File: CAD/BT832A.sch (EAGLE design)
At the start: 22 parts, among them IC1 CP2102, U2 BT832, U3 LP5907MFX-3.3/NOPB, U4 LP5907MFX-3.3/NOPB, U5 ADS131M08IPBS, X1_8.192MHZ ABM3B-8.000MHZ-B2-T, X2_32.768KHZ FC-12M

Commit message: Update BT832A.sch
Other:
- note added: "TODO: Add 2.2uF caps between + and - inputs (at least for EEG)"
- note removed: "TODO: Add 220pf caps between + and - inputs."
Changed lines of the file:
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@@
 <text x="139.7" y="142.24" size="1.778" layer="97" rot="R90">830050789</text>
 <text x="127" y="38.1" size="1.778" layer="97">MicroUSB</text>
-<text x="-12.7" y="172.72" size="1.778" layer="95">TODO:
-Add 220pf caps between + and - inputs.</text>
+<text x="-12.7" y="170.18" size="1.778" layer="95">TODO:
+Add 2.2uF caps between + and - inputs
+(at least for EEG)</text>
 <wire x1="109.22" y1="25.4" x2="109.22" y2="76.2" width="0.1524" layer="97"/>
 <wire x1="109.22" y1="76.2" x2="50.8" y2="76.2" width="0.1524" layer="97"/>

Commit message: finished sch
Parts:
- added C10: 1.0uF, adafruit:C-USC0603
- added C11: 0.1uF, adafruit:C-USC0603
- added C12, C13: 1uF, adafruit:C-USC0603
- added D1: BAT60J, diode:BAT60J
- added D2, D3: BAS40-06, diode:BAS40-06
- added LED1, LED2: (no value), adafruit:LEDCHIP-LED0603
- added R1: 4.7kΩ, adafruit:R-US_R0603
- added R2, R3: 3.3kΩ, adafruit:R-US_R0603
- added R4, R7: 10kΩ, adafruit:R-US_R0603
- added R5: 47kΩ, adafruit:R-US_R0603
- added R6: 2kΩ, adafruit:R-US_R0603
- added U1: MCP73831T-3ACI/OT, MCP73831T-3ACI_OT:MCP73831T-3ACI/OT
- added U6: BCM857BS, BCM857BS:BCM857BS
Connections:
- new net +5V: C10.2, C11.2, C7.1, D2.AA, IC1.REGIN, IC1.VBUS, U$1.1, U4.EN, U4.IN, U6.E1
- new net 10K: R4.2, U6.B1, U6.B2, U6.C1
- new net B+: D3.AA, J1.+
- new net CPRST: IC1.!RST, R1.1, U2.P08
- new net D+: IC1.D+, U$1.3
- new net D-: IC1.D-, U$1.2
- new net ID: U$1.4
- new net N$1: LED2.A, R3.1
- new net N$11: LED1.A, R2.2
- new net N$14: D2.K2, R5.1, U6.C2
- new net N$18: LED1.C, U1.STAT
- new net N$2: U2.P21/RESET
- new net N$3: LED2.C
- new net N$4: U2.VDD
- new net N$5: R3.2
- new net N$8: U3.GND
- new net N$9: R6.1, U1.PROG
- new net NVD: D1.A, D2.K1, D3.K2, R2.1, R7.2, U1.VDD, U6.E2
- new net RXD: IC1.RXD, U2.P12
- new net TXD: IC1.TXD, U2.P11
- new net VDD: C12.2, R1.2, U3.OUT
- new net VIN: C13.2, D1.C, D3.K1, U3.EN, U3.IN
- net 3V3: no longer C7.1, U4.EN, U4.IN
- net GND: now also C10.1, C11.1, C12.1, C13.1, IC1.GND, IC1.GND@EXP, IC1.GND@M, J1.-, R4.1, R5.2, R6.2, R7.1, U$1.5, U2.GND
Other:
- moved on the sheet: J1

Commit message: smaller packages
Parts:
- C10, C11, C12, C13, C5, C6, C7, C8, C9: device adafruit:C-USC0603 -> adafruit:C-USC0402
- R1, R2, R3, R4, R5, R6: device adafruit:R-US_R0603 -> adafruit:R-US_R0402
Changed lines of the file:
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@@
 <part name="J1" library="SparkFun-Connectors" library_urn="urn:adsk.eagle:library:513" deviceset="JST_2MM_MALE" device="" package3d_urn="urn:adsk.eagle:package:38042/1"/>
 <part name="U4" library="LP5907MFX-3.3_NOPB" deviceset="LP5907MFX-3.3/NOPB" device=""/>
-<part name="C5" library="adafruit" deviceset="C-US" device="C0603" value="1uF"/>
-<part name="C6" library="adafruit" deviceset="C-US" device="C0603" value="220uF"/>
-<part name="C7" library="adafruit" deviceset="C-US" device="C0603" value="1uF"/>
-<part name="C8" library="adafruit" deviceset="C-US" device="C0603" value="1uF"/>
+<part name="C5" library="adafruit" deviceset="C-US" device="C0402" value="1uF"/>
+<part name="C6" library="adafruit" deviceset="C-US" device="C0402" value="220uF"/>
+<part name="C7" library="adafruit" deviceset="C-US" device="C0402" value="1uF"/>
+<part name="C8" library="adafruit" deviceset="C-US" device="C0402" value="1uF"/>
 <part name="SV1" library="con-lsta" library_urn="urn:adsk.eagle:library:161" deviceset="FE08-2" device="" package3d_urn="urn:adsk.eagle:package:8174/1"/>
 <part name="U5" library="ADS131M08IPBS" deviceset="ADS131M08IPBS" device=""/>
-<part name="C9" library="adafruit" deviceset="C-US" device="C0603" value="100uF"/>
+<part name="C9" library="adafruit" deviceset="C-US" device="C0402" value="100uF"/>
 <part name="SJ1" library="jumper" library_urn="urn:adsk.eagle:library:252" deviceset="SJ" device="" package3d_urn="urn:adsk.eagle:package:15471/1"/>
 <part name="U$2" library="adafruit" deviceset="PINHD-1X10" device=""/>
@@
 <part name="SUPPLY1" library="supply2" library_urn="urn:adsk.eagle:library:372" deviceset="GND" device=""/>
 <part name="SUPPLY2" library="supply2" library_urn="urn:adsk.eagle:library:372" deviceset="GND" device=""/>
-<part name="C10" library="adafruit" library_urn="urn:adsk.eagle:library:420" deviceset="C-US" device="C0603" package3d_urn="urn:adsk.eagle:package:6240338/1" value="1.0uF"/>
-<part name="C11" library="adafruit" library_urn="urn:adsk.eagle:library:420" deviceset="C-US" device="C0603" package3d_urn="urn:adsk.eagle:package:6240338/1" value="0.1uF"/>
+<part name="C10" library="adafruit" library_urn="urn:adsk.eagle:library:420" deviceset="C-US" device="C0402" package3d_urn="urn:adsk.eagle:package:6240340/1" value="1.0uF"/>
+<part name="C11" library="adafruit" library_urn="urn:adsk.eagle:library:420" deviceset="C-US" device="C0402" package3d_urn="urn:adsk.eagle:package:6240340/1" value="0.1uF"/>
 <part name="P+1" library="supply1" library_urn="urn:adsk.eagle:library:371" deviceset="+5V" device=""/>
 <part name="SUPPLY3" library="supply2" library_urn="urn:adsk.eagle:library:372" deviceset="GND" device=""/>
 <part name="P+2" library="supply1" library_urn="urn:adsk.eagle:library:371" deviceset="+5V" device=""/>
 <part name="P+3" library="supply1" library_urn="urn:adsk.eagle:library:371" deviceset="+5V" device=""/>
-<part name="R1" library="adafruit" library_urn="urn:adsk.eagle:library:420" deviceset="R-US_" device="R0603" package3d_urn="urn:adsk.eagle:package:6240565/1" value="4.7kΩ"/>
-<part name="C12" library="adafruit" deviceset="C-US" device="C0603" value="1uF"/>
-<part name="C13" library="adafruit" deviceset="C-US" device="C0603" value="1uF"/>
+<part name="R1" library="adafruit" library_urn="urn:adsk.eagle:library:420" deviceset="R-US_" device="R0402" package3d_urn="urn:adsk.eagle:package:6240564/1" value="4.7kΩ"/>
+<part name="C12" library="adafruit" deviceset="C-US" device="C0402" value="1uF"/>
+<part name="C13" library="adafruit" deviceset="C-US" device="C0402" value="1uF"/>
 <part name="SUPPLY4" library="supply2" library_urn="urn:adsk.eagle:library:372" deviceset="GND" device=""/>
 <part name="U1" library="MCP73831T-3ACI_OT" deviceset="MCP73831T-3ACI/OT" device=""/>
@@
 <part name="LED1" library="adafruit" library_urn="urn:adsk.eagle:library:420" deviceset="LED" device="CHIP-LED0603" package3d_urn="urn:adsk.eagle:package:6240556/1"/>
 <part name="LED2" library="adafruit" library_urn="urn:adsk.eagle:library:420" deviceset="LED" device="CHIP-LED0603" package3d_urn="urn:adsk.eagle:package:6240556/1"/>
-<part name="R2" library="adafruit" library_urn="urn:adsk.eagle:library:420" deviceset="R-US_" device="R0603" package3d_urn="urn:adsk.eagle:package:6240565/1" value="3.3kΩ"/>
-<part name="R3" library="adafruit" library_urn="urn:adsk.eagle:library:420" deviceset="R-US_" device="R0603" package3d_urn="urn:adsk.eagle:package:6240565/1" value="3.3kΩ"/>
-<part name="R4" library="adafruit" library_urn="urn:adsk.eagle:library:420" deviceset="R-US_" device="R0603" package3d_urn="urn:adsk.eagle:package:6240565/1" value="10kΩ"/>
-<part name="R5" library="adafruit" library_urn="urn:adsk.eagle:library:420" deviceset="R-US_" device="R0603" package3d_urn="urn:adsk.eagle:package:6240565/1" value="47kΩ"/>
-<part name="R6" library="adafruit" library_urn="urn:adsk.eagle:library:420" deviceset="R-US_" device="R0603" package3d_urn="urn:adsk.eagle:package:6240565/1" value="2kΩ"/>
+<part name="R2" library="adafruit" library_urn="urn:adsk.eagle:library:420" deviceset="R-US_" device="R0402" package3d_urn="urn:adsk.eagle:package:6240564/1" value="3.3kΩ"/>
+<part name="R3" library="adafruit" library_urn="urn:adsk.eagle:library:420" deviceset="R-US_" device="R0402" package3d_urn="urn:adsk.eagle:package:6240564/1" value="3.3kΩ"/>
+<part name="R4" library="adafruit" library_urn="urn:adsk.eagle:library:420" deviceset="R-US_" device="R0402" package3d_urn="urn:adsk.eagle:package:6240564/1" value="10kΩ"/>
+<part name="R5" library="adafruit" library_urn="urn:adsk.eagle:library:420" deviceset="R-US_" device="R0402" package3d_urn="urn:adsk.eagle:package:6240564/1" value="47kΩ"/>
+<part name="R6" library="adafruit" library_urn="urn:adsk.eagle:library:420" deviceset="R-US_" device="R0402" package3d_urn="urn:adsk.eagle:package:6240564/1" value="2kΩ"/>
 <part name="P+4" library="supply1" library_urn="urn:adsk.eagle:library:371" deviceset="+5V" device=""/>
 <part name="SUPPLY5" library="supply2" library_urn="urn:adsk.eagle:library:372" deviceset="GND" device=""/>

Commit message: edits
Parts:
- renumbered X1_8.192MHZ to X1, X2_32.768KHZ to X2
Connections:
- new net SWDCLK: U2.SWDCLK
- new net SWDIO: U2.SWDIO
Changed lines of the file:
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@@
 <part name="U2" library="BT832" deviceset="BT832" device=""/>
 <part name="U3" library="LP5907MFX-3.3_NOPB" deviceset="LP5907MFX-3.3/NOPB" device=""/>
-<part name="X2_32.768KHZ" library="crystal" library_urn="urn:adsk.eagle:library:204" deviceset="FC-12M" device="" package3d_urn="urn:adsk.eagle:package:12123/1"/>
-<part name="X1_8.192MHZ" library="Crystals_Oscillators" library_urn="urn:adsk.eagle:library:24014151" deviceset="ABM3B-8.000MHZ-B2-T" device="" package3d_urn="urn:adsk.eagle:package:10899604/4"/>
+<part name="X2" library="crystal" library_urn="urn:adsk.eagle:library:204" deviceset="FC-12M" device="" package3d_urn="urn:adsk.eagle:package:12123/1"/>
+<part name="X1" library="Crystals_Oscillators" library_urn="urn:adsk.eagle:library:24014151" deviceset="ABM3B-8.000MHZ-B2-T" device="" package3d_urn="urn:adsk.eagle:package:10899604/4"/>
 <part name="C1" library="adafruit" library_urn="urn:adsk.eagle:library:420" deviceset="C-US" device="C0402" package3d_urn="urn:adsk.eagle:package:6240340/1"/>
 <part name="C2" library="adafruit" library_urn="urn:adsk.eagle:library:420" deviceset="C-US" device="C0402" package3d_urn="urn:adsk.eagle:package:6240340/1"/>
@@
 <attribute name="VALUE" x="68.58" y="102.68" size="2.0828" layer="96" ratio="10" rot="SR0"/>
 </instance>
-<instance part="X2_32.768KHZ" gate="G$1" x="142.24" y="147.32" smashed="yes" rot="R90">
+<instance part="X2" gate="G$1" x="142.24" y="147.32" smashed="yes" rot="R90">
 <attribute name="NAME" x="136.144" y="139.7" size="1.778" layer="95" rot="R90"/>
 </instance>
-<instance part="X1_8.192MHZ" gate="G$1" x="-5.08" y="88.9" smashed="yes">
+<instance part="X1" gate="G$1" x="-5.08" y="88.9" smashed="yes">
 <attribute name="NAME" x="-8.128" y="69.85" size="1.778" layer="95"/>
 </instance>
@@
 </segment>
 <segment>
-<pinref part="X1_8.192MHZ" gate="G$1" pin="4"/>
+<pinref part="X1" gate="G$1" pin="4"/>
 <wire x1="0" y1="83.82" x2="0" y2="81.28" width="0.1524" layer="91"/>
 <label x="0" y="81.28" size="1.778" layer="95" rot="R270"/>
 </segment>
 <segment>
-<pinref part="X1_8.192MHZ" gate="G$1" pin="2"/>
+<pinref part="X1" gate="G$1" pin="2"/>
 <wire x1="-2.54" y1="83.82" x2="-2.54" y2="81.28" width="0.1524" layer="91"/>
 <label x="-2.54" y="81.28" size="1.778" layer="95" rot="R270"/>
@@
 </segment>
 <segment>
-<pinref part="X1_8.192MHZ" gate="G$1" pin="3"/>
+<pinref part="X1" gate="G$1" pin="3"/>
 <wire x1="5.08" y1="88.9" x2="7.62" y2="88.9" width="0.1524" layer="91"/>
 <label x="5.08" y="91.44" size="1.778" layer="95"/>
@@
 </segment>
 <segment>
-<pinref part="X1_8.192MHZ" gate="G$1" pin="1"/>
+<pinref part="X1" gate="G$1" pin="1"/>
 <wire x1="-7.62" y1="88.9" x2="-10.16" y2="88.9" width="0.1524" layer="91"/>
 <label x="-12.7" y="91.44" size="1.778" layer="95"/>
@@
 </segment>
 <segment>
-<pinref part="X2_32.768KHZ" gate="G$1" pin="2"/>
+<pinref part="X2" gate="G$1" pin="2"/>
 <wire x1="142.24" y1="149.86" x2="142.24" y2="152.4" width="0.1524" layer="91"/>
 <label x="142.24" y="152.4" size="1.778" layer="95"/>
@@
 </segment>
 <segment>
-<pinref part="X2_32.768KHZ" gate="G$1" pin="1"/>
+<pinref part="X2" gate="G$1" pin="1"/>
 <wire x1="142.24" y1="144.78" x2="142.24" y2="142.24" width="0.1524" layer="91"/>
 <label x="142.24" y="139.7" size="1.778" layer="95"/>
@@
 </segment>
 </net>
+<net name="SWDIO" class="0">
+<segment>
+<pinref part="U2" gate="G$1" pin="SWDIO"/>
+<wire x1="157.48" y1="101.6" x2="153.924" y2="101.6" width="0.1524" layer="91"/>
+<label x="144.526" y="100.838" size="1.778" layer="95"/>
+</segment>
+</net>
+<net name="SWDCLK" class="0">
+<segment>
+<pinref part="U2" gate="G$1" pin="SWDCLK"/>
+<wire x1="157.48" y1="104.14" x2="153.924" y2="104.14" width="0.1524" layer="91"/>
+<label x="142.748" y="103.378" size="1.778" layer="95"/>
+</segment>
+</net>

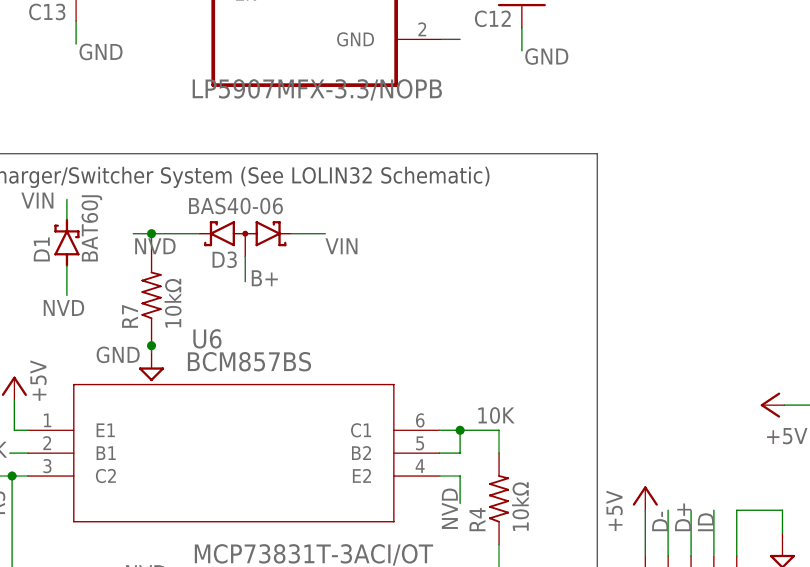
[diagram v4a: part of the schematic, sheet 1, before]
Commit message: add switch
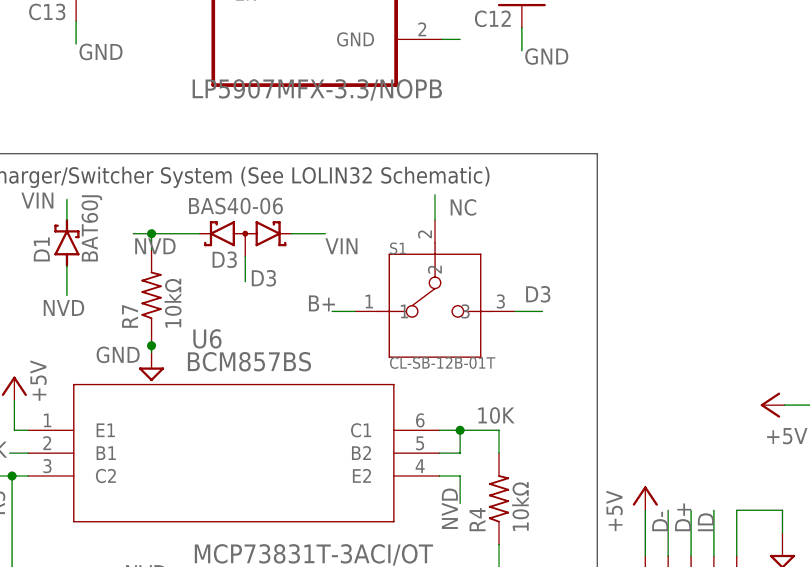
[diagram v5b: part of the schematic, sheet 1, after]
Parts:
- added S1: CL-SB-12B-01T, CL-SB-12B-01T:CL-SB-12B-01T
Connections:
- new net D3: D3.AA, S1.3
- net B+: now also S1.1; no longer D3.AA
- net NC: now also S1.2
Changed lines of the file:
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@@
 <part name="SUPPLY9" library="supply2" library_urn="urn:adsk.eagle:library:372" deviceset="GND" device=""/>
 <part name="P+5" library="supply1" library_urn="urn:adsk.eagle:library:371" deviceset="+5V" device=""/>
+<part name="S1" library="CL-SB-12B-01T" deviceset="CL-SB-12B-01T" device=""/>
 </parts>
 <sheets>
@@
 <attribute name="VALUE" x="52.578" y="68.834" size="1.778" layer="96" rot="R90"/>
 </instance>
+<instance part="S1" gate="A" x="95.758" y="78.994" smashed="yes">
+<attribute name="NAME" x="90.66451875" y="85.36085" size="1.27336875" layer="95" ratio="10"/>
+<attribute name="VALUE" x="90.66936875" y="72.633209375" size="1.27215" layer="96" ratio="10"/>
+</instance>
 </instances>
 <busses>
@@
 <label x="-46.99" y="108.966" size="1.778" layer="95"/>
 </segment>
+<segment>
+<pinref part="S1" gate="A" pin="2"/>
+<wire x1="95.758" y1="89.154" x2="95.758" y2="91.948" width="0.1524" layer="91"/>
+<label x="97.282" y="89.662" size="1.778" layer="95"/>
+</segment>
 </net>
 <net name="CAP" class="0">
@@
 </segment>
 <segment>
+<pinref part="S1" gate="A" pin="1"/>
+<wire x1="86.868" y1="78.994" x2="84.328" y2="78.994" width="0.1524" layer="91"/>
+<label x="81.534" y="78.994" size="1.778" layer="95"/>
+</segment>
+</net>
+<net name="VIN" class="0">
+<segment>
+<pinref part="U3" gate="G$1" pin="IN"/>
+<wire x1="66.04" y1="119.38" x2="63.754" y2="119.38" width="0.1524" layer="91"/>
+<label x="60.452" y="119.634" size="1.778" layer="95"/>
+</segment>
+<segment>
+<pinref part="U3" gate="G$1" pin="EN"/>
+<wire x1="66.04" y1="114.3" x2="63.754" y2="114.3" width="0.1524" layer="91"/>
+<label x="60.452" y="115.062" size="1.778" layer="95"/>
+</segment>
+<segment>
+<pinref part="D3" gate="G$1" pin="K1"/>
+<wire x1="79.756" y1="87.63" x2="83.566" y2="87.63" width="0.1524" layer="91"/>
+<label x="83.566" y="85.344" size="1.778" layer="95"/>
+</segment>
+<segment>
+<pinref part="D1" gate="G$1" pin="C"/>
+<wire x1="54.864" y1="89.154" x2="54.864" y2="91.44" width="0.1524" layer="91"/>
+<label x="49.784" y="90.424" size="1.778" layer="95"/>
+</segment>
+<segment>
+<pinref part="C13" gate="G$1" pin="2"/>
+<wire x1="55.88" y1="118.872" x2="55.88" y2="121.158" width="0.1524" layer="91"/>
+<label x="54.102" y="121.92" size="1.778" layer="95"/>
+</segment>
+</net>
+<net name="SWDIO" class="0">
+<segment>
+<pinref part="U2" gate="G$1" pin="SWDIO"/>
+<wire x1="157.48" y1="101.6" x2="153.924" y2="101.6" width="0.1524" layer="91"/>
+<label x="144.526" y="100.838" size="1.778" layer="95"/>
+</segment>
+</net>
+<net name="SWDCLK" class="0">
+<segment>
+<pinref part="U2" gate="G$1" pin="SWDCLK"/>
+<wire x1="157.48" y1="104.14" x2="153.924" y2="104.14" width="0.1524" layer="91"/>
+<label x="142.748" y="103.378" size="1.778" layer="95"/>
+</segment>
+</net>
+<net name="D3" class="0">
+<segment>
 <pinref part="D3" gate="G$1" pin="AA"/>
 <wire x1="74.676" y1="85.09" x2="74.676" y2="82.296" width="0.1524" layer="91"/>
 <label x="75.184" y="81.788" size="1.778" layer="95"/>
 </segment>
-</net>
-<net name="VIN" class="0">
-<segment>
-<pinref part="U3" gate="G$1" pin="IN"/>
-<wire x1="66.04" y1="119.38" x2="63.754" y2="119.38" width="0.1524" layer="91"/>
-<label x="60.452" y="119.634" size="1.778" layer="95"/>
-</segment>
-<segment>
-<pinref part="U3" gate="G$1" pin="EN"/>
-<wire x1="66.04" y1="114.3" x2="63.754" y2="114.3" width="0.1524" layer="91"/>
-<label x="60.452" y="115.062" size="1.778" layer="95"/>
-</segment>
-<segment>
-<pinref part="D3" gate="G$1" pin="K1"/>
-<wire x1="79.756" y1="87.63" x2="83.566" y2="87.63" width="0.1524" layer="91"/>
-<label x="83.566" y="85.344" size="1.778" layer="95"/>
-</segment>
-<segment>
-<pinref part="D1" gate="G$1" pin="C"/>
-<wire x1="54.864" y1="89.154" x2="54.864" y2="91.44" width="0.1524" layer="91"/>
-<label x="49.784" y="90.424" size="1.778" layer="95"/>
-</segment>
-<segment>
-<pinref part="C13" gate="G$1" pin="2"/>
-<wire x1="55.88" y1="118.872" x2="55.88" y2="121.158" width="0.1524" layer="91"/>
-<label x="54.102" y="121.92" size="1.778" layer="95"/>
-</segment>
-</net>
-<net name="SWDIO" class="0">
-<segment>
-<pinref part="U2" gate="G$1" pin="SWDIO"/>
-<wire x1="157.48" y1="101.6" x2="153.924" y2="101.6" width="0.1524" layer="91"/>
-<label x="144.526" y="100.838" size="1.778" layer="95"/>
-</segment>
-</net>
-<net name="SWDCLK" class="0">
-<segment>
-<pinref part="U2" gate="G$1" pin="SWDCLK"/>
-<wire x1="157.48" y1="104.14" x2="153.924" y2="104.14" width="0.1524" layer="91"/>
-<label x="142.748" y="103.378" size="1.778" layer="95"/>
-</segment>
-</net>
+<segment>
+<pinref part="S1" gate="A" pin="3"/>
+<wire x1="104.648" y1="78.994" x2="107.696" y2="78.994" width="0.1524" layer="91"/>
+<label x="105.664" y="80.01" size="1.778" layer="95"/>
+</segment>
+</net>
